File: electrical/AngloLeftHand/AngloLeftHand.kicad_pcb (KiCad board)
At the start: 2 copper layers, 82 x 60 mm, 49 parts, among them J3 TC2030-NL, U1 DRV5053VAQDBZR, U10 DRV5053VAQDBZR, U11 DRV5053VAQDBZR, U12 DRV5053VAQDBZR, U13 DRV5053VAQDBZR, U14 DRV5053VAQDBZR, U15 DRV5053VAQDBZR, U16 STM32L072CBTx, U17 CD74HC4067SM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

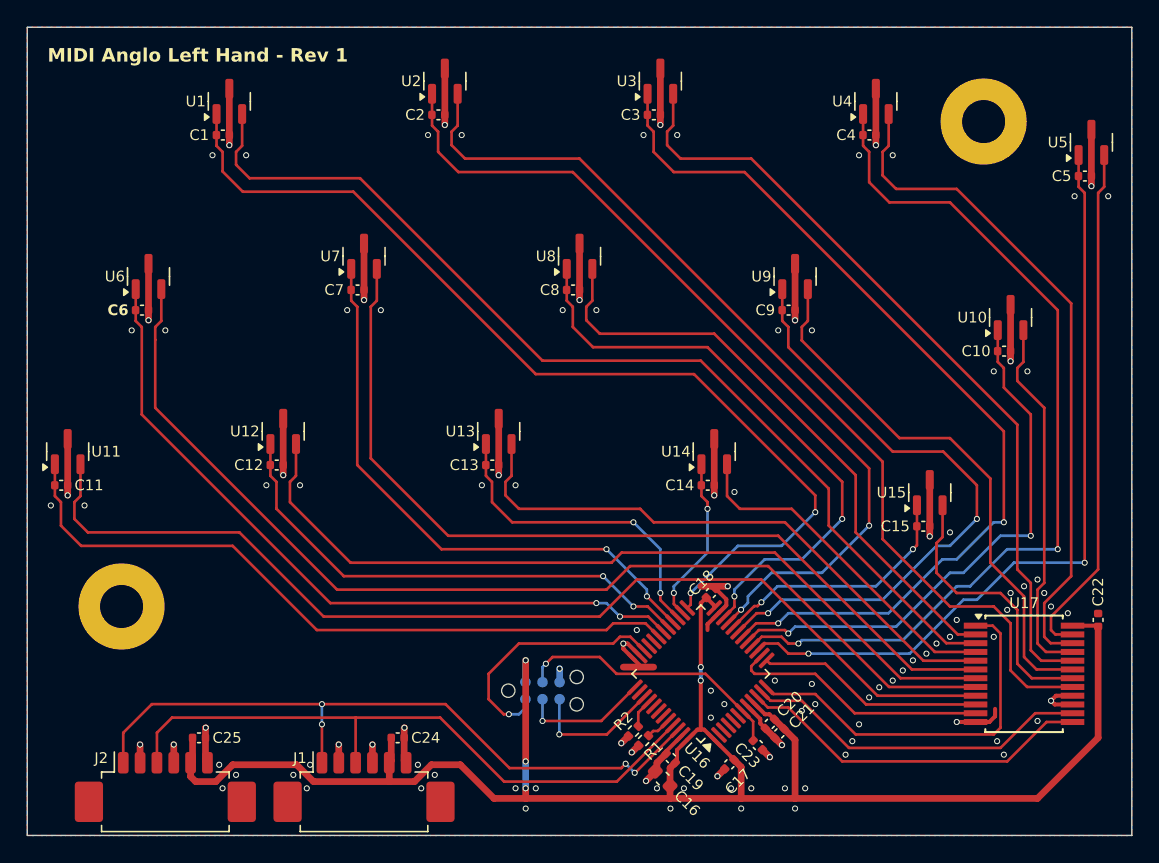
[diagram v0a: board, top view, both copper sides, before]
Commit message: Add stitching vias
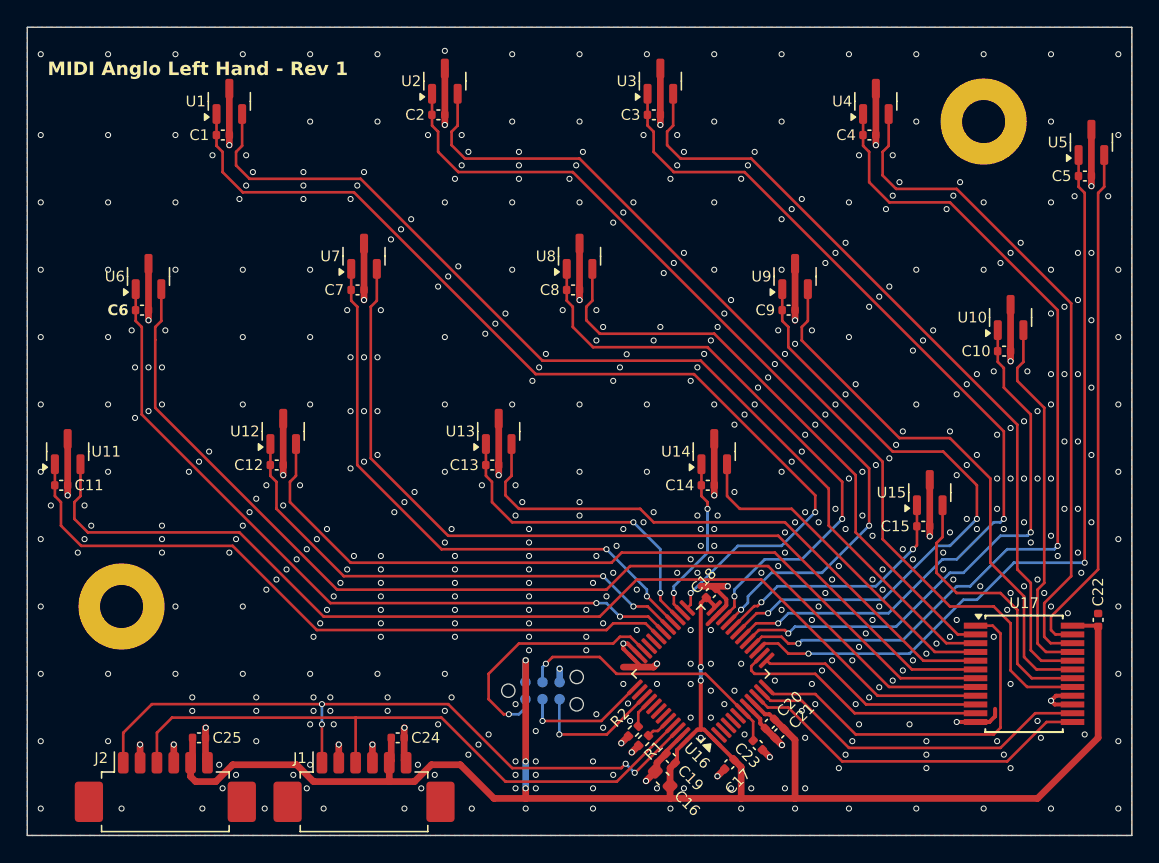
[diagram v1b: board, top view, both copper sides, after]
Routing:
- net GND: track 104.6 -> 104.5 mm, vias 112 -> 549

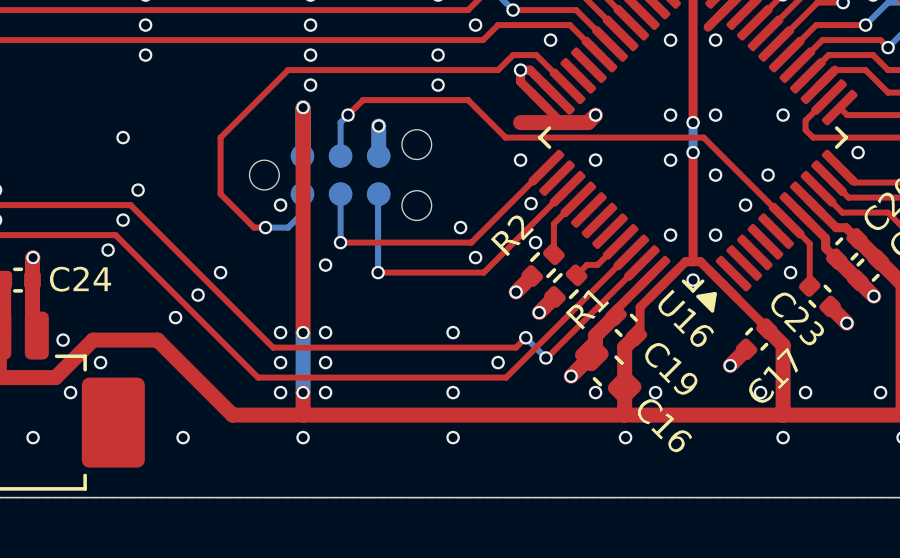
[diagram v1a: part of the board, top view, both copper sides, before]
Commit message: Swap SDA and SCL on button board connectors
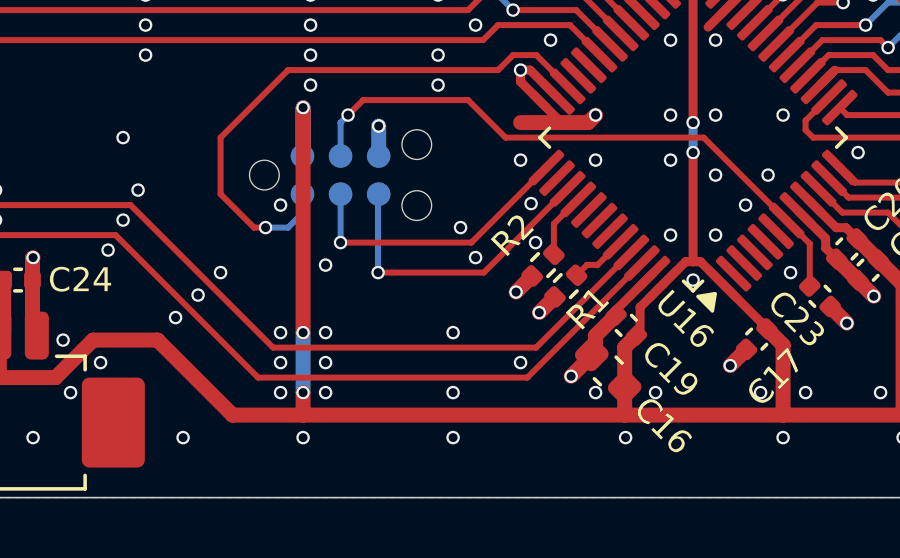
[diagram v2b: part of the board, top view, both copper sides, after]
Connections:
- J1 pad 1: I2C_SDA -> I2C_SCL
- J1 pad 3: I2C_SCL -> I2C_SDA
- J2 pad 1: I2C_SDA -> I2C_SCL
- J2 pad 3: I2C_SCL -> I2C_SDA
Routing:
- net I2C_SDA: track 52.3 -> 48.3 mm, vias 4 -> 0
- net I2C_SCL: track 48.1 -> 51.6 mm, vias 0 -> 2
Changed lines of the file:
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@@
 			(layers "F.Cu" "F.Mask" "F.Paste")
 			(roundrect_rratio 0.25)
-			(net 15 "I2C_SDA")
+			(net 14 "I2C_SCL")
 			(pinfunction "Pin_1")
 			(pintype "passive")
@@
 			(layers "F.Cu" "F.Mask" "F.Paste")
 			(roundrect_rratio 0.25)
-			(net 14 "I2C_SCL")
+			(net 15 "I2C_SDA")
 			(pinfunction "Pin_3")
 			(pintype "passive")
@@
 			(layers "F.Cu" "F.Mask" "F.Paste")
 			(roundrect_rratio 0.25)
-			(net 15 "I2C_SDA")
+			(net 14 "I2C_SCL")
 			(pinfunction "Pin_1")
 			(pintype "passive")
@@
 			(layers "F.Cu" "F.Mask" "F.Paste")
 			(roundrect_rratio 0.25)
-			(net 14 "I2C_SCL")
+			(net 15 "I2C_SDA")
 			(pinfunction "Pin_3")
 			(pintype "passive")
@@
 	)
 	(via
-		(at 82.5 158.5)
+		(at 83.25 158.5)
 		(size 0.45)
 		(drill 0.3)
@@
 	)
 	(segment
-		(start 48.625 157.6)
-		(end 48.625 155.375)
-		(width 0.2)
-		(layer "F.Cu")
-		(net 14)
-	)
-	(segment
-		(start 82.767767 159)
-		(end 86.940552 154.827215)
+		(start 75 158)
+		(end 70.25 153.25)
 		(width 0.2)
 		(layer "F.Cu")
@@
 	)
 	(segment
-		(start 48.625 155.375)
-		(end 49.75 154.25)
+		(start 48.25 153.25)
+		(end 46.125 155.375)
 		(width 0.2)
 		(layer "F.Cu")
@@
 	)
 	(segment
-		(start 74.5 159)
-		(end 82.767767 159)
+		(start 60.875 154.75)
+		(end 60.875 157.6)
 		(width 0.2)
 		(layer "F.Cu")
@@
 	)
 	(segment
-		(start 63.375 157.6)
-		(end 63.375 154.25)
+		(start 86.940551 154.827215)
+		(end 83.767766 158)
 		(width 0.2)
 		(layer "F.Cu")
@@
 	)
 	(segment
-		(start 49.75 154.25)
-		(end 69.75 154.25)
+		(start 60.875 153.25)
+		(end 48.25 153.25)
 		(width 0.2)
 		(layer "F.Cu")
@@
 	)
 	(segment
-		(start 69.75 154.25)
-		(end 74.5 159)
+		(start 46.125 155.375)
+		(end 46.125 157.6)
 		(width 0.2)
 		(layer "F.Cu")
@@
 		(width 0.2)
 		(layer "F.Cu")
-		(net 15)
+		(net 14)
 	)
 	(segment
-		(start 48.25 153.25)
-		(end 46.125 155.375)
+		(start 83.767766 158)
+		(end 75 158)
 		(width 0.2)
 		(layer "F.Cu")
-		(net 15)
+		(net 14)
+	)
+	(via
+		(at 60.875 153.25)
+		(size 0.45)
+		(drill 0.3)
+		(layers "F.Cu" "B.Cu")
+		(net 14)
+	)
+	(via
+		(at 60.875 154.75)
+		(size 0.45)
+		(drill 0.3)
+		(layers "F.Cu" "B.Cu")
+		(net 14)
 	)
 	(segment
 		(start 60.875 154.75)
-		(end 60.875 157.6)
+		(end 60.875 153.25)
 		(width 0.2)
-		(layer "F.Cu")
-		(net 15)
+		(layer "B.Cu")
+		(net 14)
 	)
 	(segment
-		(start 84.094759 158.34476)
-		(end 84.130113 158.34476)
+		(start 74.5 159)
+		(end 83.474874 159)
 		(width 0.2)
 		(layer "F.Cu")
@@
 	)
 	(segment
-		(start 83.096015 158)
-		(end 75 158)
+		(start 69.75 154.25)
+		(end 74.5 159)
 		(width 0.2)
 		(layer "F.Cu")
@@
 	)
 	(segment
-		(start 83.423007 157.673007)
-		(end 83.096015 158)
+		(start 48.625 155.375)
+		(end 49.75 154.25)
 		(width 0.2)
 		(layer "F.Cu")
@@
 	)
 	(segment
-		(start 60.875 153.25)
-		(end 48.25 153.25)
+		(start 48.625 157.6)
+		(end 48.625 155.375)
 		(width 0.2)
 		(layer "F.Cu")
@@
 	)
 	(segment
-		(start 46.125 155.375)
-		(end 46.125 157.6)
+		(start 83.474874 159)
+		(end 87.294105 155.180769)
 		(width 0.2)
 		(layer "F.Cu")
@@
 	)
 	(segment
-		(start 84.130113 158.34476)
-		(end 87.294105 155.180768)
+		(start 63.375 157.6)
+		(end 63.375 154.25)
 		(width 0.2)
 		(layer "F.Cu")
@@
 	)
 	(segment
-		(start 75 158)
-		(end 70.25 153.25)
+		(start 49.75 154.25)
+		(end 69.75 154.25)
 		(width 0.2)
 		(layer "F.Cu")
 		(net 15)
 	)
-	(via
-		(at 60.875 153.25)
-		(size 0.45)
-		(drill 0.3)
-		(layers "F.Cu" "B.Cu")
-		(net 15)
-	)
-	(via
-		(at 84.094759 158.34476)
-		(size 0.45)
-		(drill 0.3)
-		(layers "F.Cu" "B.Cu")
-		(net 15)
-	)
-	(via
-		(at 60.875 154.75)
-		(size 0.45)
-		(drill 0.3)
-		(layers "F.Cu" "B.Cu")
-		(net 15)
-	)
-	(via
-		(at 83.423007 157.673007)
-		(size 0.45)
-		(drill 0.3)
-		(layers "F.Cu" "B.Cu")
-		(net 15)
-	)
-	(segment
-		(start 60.875 154.75)
-		(end 60.875 153.25)
-		(width 0.2)
-		(layer "B.Cu")
-		(net 15)
-	)
-	(segment
-		(start 83.423007 157.673008)
-		(end 83.423007 157.673007)
-		(width 0.2)
-		(layer "B.Cu")
-		(net 15)
-	)
-	(segment
-		(start 84.094759 158.34476)
-		(end 83.423007 157.673008)
-		(width 0.2)
-		(layer "B.Cu")
-		(net 15)
-	)

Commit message: PCB adjustments
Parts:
- H1, H2: footprint MountingHole:MountingHole_3.2mm_M3_Pad -> MountingHole:MountingHole_3.2mm_M3
- moved C25 0.25 mm to (51.5, 155.8)
- moved J2 0.25 mm to (49.0, 160.0)
